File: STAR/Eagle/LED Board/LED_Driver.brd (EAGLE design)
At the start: 30.5 x 6.6 mm, 8 parts

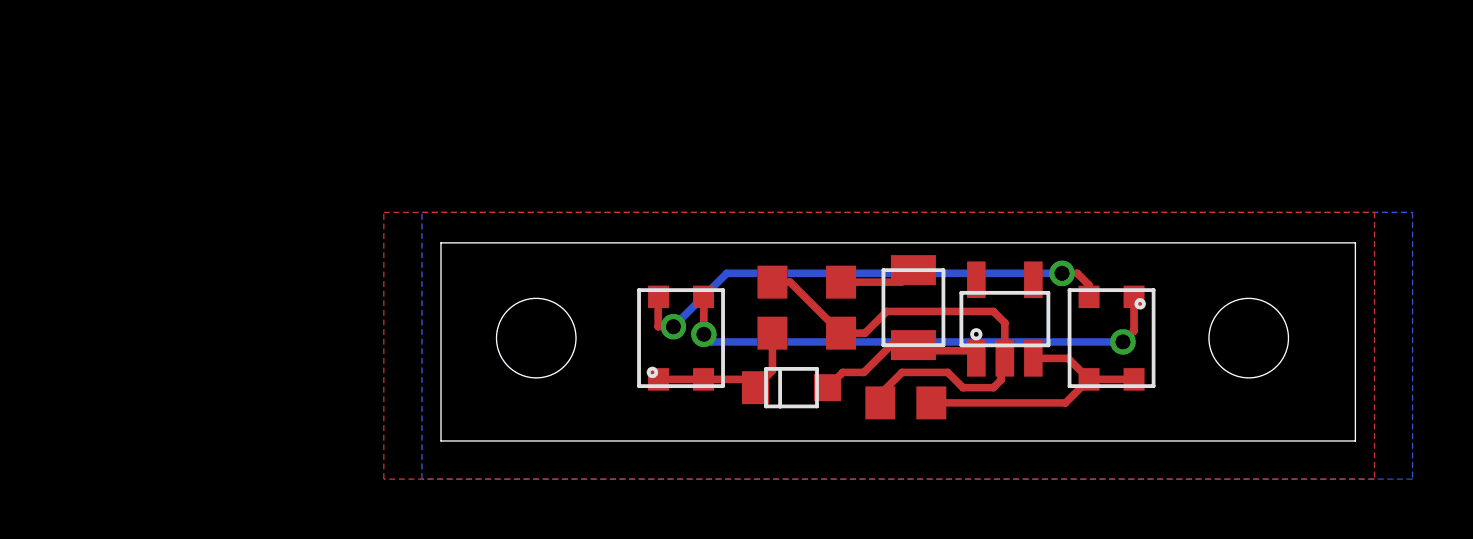
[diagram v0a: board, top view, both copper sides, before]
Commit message: LED board, added text
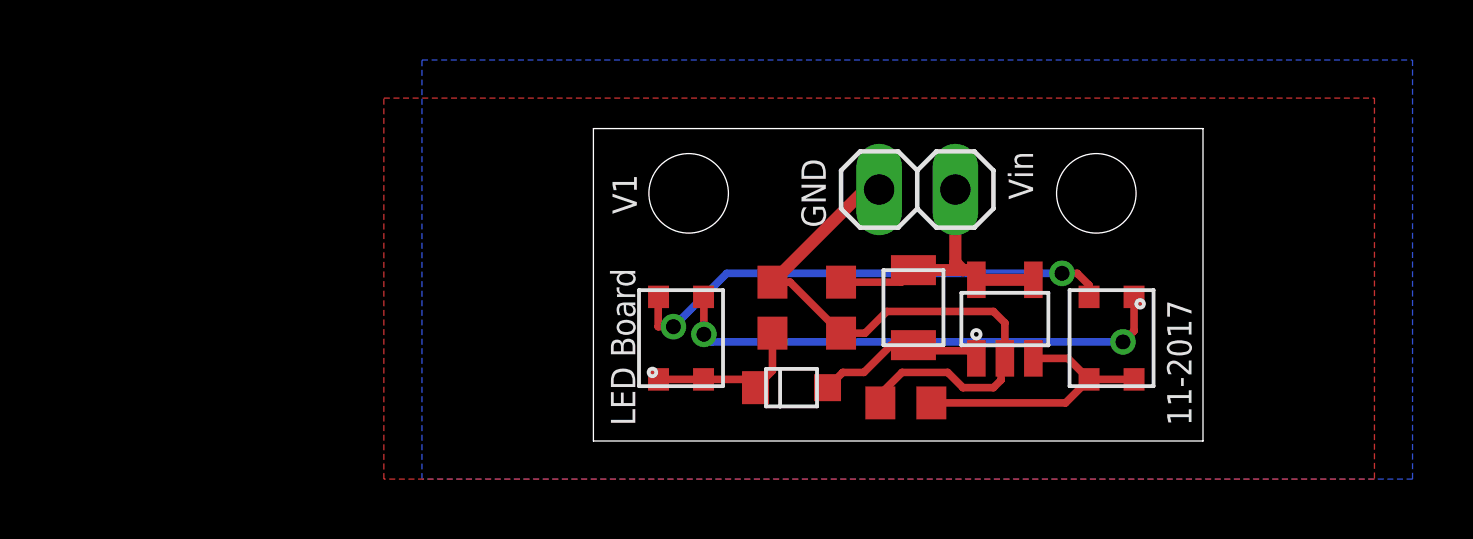
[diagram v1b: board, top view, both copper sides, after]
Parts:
- added JP1: (no value), pinhead:1X02
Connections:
- net +3V3: now also JP1.2
- net GND: now also JP1.1
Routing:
- net +3V3: track 2.91 -> 9.63 mm
- net GND: track 16.2 -> 21.0 mm
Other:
- board size 30.5 x 6.6 mm -> 20.3 x 10.4 mm
- board text added: "11-2017"
- board text added: "GND"
- board text added: "LED Board"
- board text added: "V1"
- board text added: "Vin"
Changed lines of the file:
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@@
 <layer number="98" name="Guide" color="6" fill="1" visible="no" active="no"/>
 <layer number="99" name="SpiceOrder" color="5" fill="1" visible="no" active="no"/>
+<layer number="200" name="200bmp" color="1" fill="10" visible="yes" active="yes"/>
 </layers>
 <board>
 <plain>
-<wire x1="5.715" y1="0" x2="36.195" y2="0" width="0" layer="20"/>
-<wire x1="36.195" y1="0" x2="36.195" y2="6.604" width="0" layer="20"/>
-<wire x1="36.195" y1="6.604" x2="5.715" y2="6.604" width="0" layer="20"/>
-<wire x1="5.715" y1="6.604" x2="5.715" y2="0" width="0" layer="20"/>
-<hole x="8.89" y="3.429" drill="2.65"/>
-<hole x="32.639" y="3.429" drill="2.65"/>
+<wire x1="10.795" y1="0" x2="31.115" y2="0" width="0" layer="20"/>
+<wire x1="31.115" y1="0" x2="31.115" y2="10.414" width="0" layer="20"/>
+<wire x1="31.115" y1="10.414" x2="10.795" y2="10.414" width="0" layer="20"/>
+<wire x1="10.795" y1="10.414" x2="10.795" y2="0" width="0" layer="20"/>
+<hole x="13.97" y="8.255" drill="2.65"/>
+<hole x="27.559" y="8.255" drill="2.65"/>
+<text x="24.638" y="9.652" size="0.8128" layer="21" font="vector" rot="R270">Vin</text>
+<text x="18.542" y="7.112" size="0.8128" layer="21" font="vector" rot="R90">GND</text>
+<text x="12.192" y="0.508" size="0.8128" layer="21" font="vector" rot="R90">LED Board</text>
+<text x="11.43" y="8.89" size="0.8128" layer="21" font="vector" rot="R270">V1</text>
+<text x="30.734" y="0.508" size="0.8128" layer="21" font="vector" rot="R90">11-2017</text>
 </plain>
 <attributes>
@@
 <element name="U$4" library="LED" package="CLA2A-WKW-CYBZ0343CT" value="CLA2A-WKW-CYBZ0343CT" x="13.716" y="3.429" smashed="yes" rot="R90"/>
 <element name="U$5" library="LED" package="CLA2A-WKW-CYBZ0343CT" value="CLA2A-WKW-CYBZ0343CT" x="28.067" y="3.429" smashed="yes" rot="R270"/>
+<element name="JP1" library="pinhead" package="1X02" value="" x="21.59" y="8.382" smashed="yes">
+<attribute name="VALUE" x="19.05" y="5.207" size="1.27" layer="27"/>
+</element>
 </elements>
 <signals>
@@
 <wire x1="21.063" y1="5.295" x2="21.463" y2="5.695" width="0.254" layer="1"/>
 <wire x1="23.494" y1="5.695" x2="23.561" y2="5.374" width="0.254" layer="1"/>
-<wire x1="23.561" y1="5.374" x2="25.461" y2="5.374" width="0" layer="19" extent="1-1"/>
-<wire x1="21.463" y1="5.695" x2="23.494" y2="5.695" width="0" layer="19" extent="1-1"/>
+<wire x1="23.494" y1="5.695" x2="23.114" y2="5.695" width="0.4064" layer="1"/>
+<wire x1="23.114" y1="5.695" x2="21.463" y2="5.695" width="0.4064" layer="1"/>
+<wire x1="23.561" y1="5.374" x2="25.461" y2="5.374" width="0.4064" layer="1"/>
+<contactref element="JP1" pad="2"/>
+<wire x1="22.86" y1="8.382" x2="22.86" y2="5.949" width="0.4064" layer="1"/>
+<wire x1="22.86" y1="5.949" x2="23.114" y2="5.695" width="0.4064" layer="1"/>
 </signal>
 <signal name="GND">
@@
 <wire x1="24.384" y1="2.627" x2="24.511" y2="2.754" width="0.254" layer="1"/>
 <polygon width="0.254" layer="16">
-<vertex x="5.08" y="7.62"/>
-<vertex x="38.1" y="7.62"/>
+<vertex x="5.08" y="12.7"/>
+<vertex x="38.1" y="12.7"/>
 <vertex x="38.1" y="-1.27"/>
 <vertex x="5.08" y="-1.27"/>
 </polygon>
 <polygon width="0.254" layer="1">
-<vertex x="3.81" y="7.62"/>
-<vertex x="36.83" y="7.62"/>
+<vertex x="3.81" y="11.43"/>
+<vertex x="36.83" y="11.43"/>
 <vertex x="36.83" y="-1.27"/>
 <vertex x="3.81" y="-1.27"/>
 </polygon>
+<contactref element="JP1" pad="1"/>
+<wire x1="20.32" y1="8.382" x2="19.851" y2="8.382" width="0.4064" layer="1"/>
+<wire x1="19.851" y1="8.382" x2="16.764" y2="5.295" width="0.4064" layer="1"/>
 </signal>
 <signal name="N$1">

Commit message: screws
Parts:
- C1: value (none) -> .1uF
- C2: value (none) -> 22uF
- R1: value (none) -> 4.75
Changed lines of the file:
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@@
 <wire x1="31.115" y1="10.414" x2="10.795" y2="10.414" width="0" layer="20"/>
 <wire x1="10.795" y1="10.414" x2="10.795" y2="0" width="0" layer="20"/>
-<hole x="13.97" y="8.255" drill="2.65"/>
-<hole x="27.559" y="8.255" drill="2.65"/>
+<hole x="13.97" y="8.255" drill="2.1"/>
+<hole x="27.559" y="8.255" drill="2.1"/>
 <text x="24.638" y="9.652" size="0.8128" layer="21" font="vector" rot="R270">Vin</text>
 <text x="18.542" y="7.112" size="0.8128" layer="21" font="vector" rot="R90">GND</text>
@@
 <text x="11.43" y="8.89" size="0.8128" layer="21" font="vector" rot="R270">V1</text>
 <text x="30.734" y="0.508" size="0.8128" layer="21" font="vector" rot="R90">11-2017</text>
+<circle x="13.97" y="8.255" radius="1.9" width="0.4064" layer="51"/>
+<circle x="27.559" y="8.255" radius="1.9" width="0.4064" layer="51"/>
 </plain>
 <attributes>
@@
 </autorouter>
 <elements>
-<element name="C1" library="resistor" package="C0603" value="" x="16.764" y="4.445" smashed="yes" rot="R90">
+<element name="C1" library="resistor" package="C0603" value=".1uF" x="16.764" y="4.445" smashed="yes" rot="R90">
 <attribute name="VALUE" x="18.669" y="3.81" size="1.27" layer="27" rot="R90"/>
 </element>
-<element name="C2" library="resistor" package="C0603" value="" x="19.05" y="4.445" smashed="yes" rot="R270">
+<element name="C2" library="resistor" package="C0603" value="22uF" x="19.05" y="4.445" smashed="yes" rot="R270">
 <attribute name="VALUE" x="17.145" y="5.08" size="1.27" layer="27" rot="R270"/>
 </element>
-<element name="R1" library="resistor" package="R0603" value="" x="21.209" y="1.27" smashed="yes">
+<element name="R1" library="resistor" package="R0603" value="4.75" x="21.209" y="1.27" smashed="yes">
 <attribute name="VALUE" x="20.574" y="-0.635" size="1.27" layer="27"/>
 </element>

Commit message: misc board stuff
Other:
- board text added: "1-2018"
- board text added: "V1.1"
- board text removed: "11-2017"
- board text removed: "V1"
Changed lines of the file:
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@@
 <text x="18.542" y="7.112" size="0.8128" layer="21" font="vector" rot="R90">GND</text>
 <text x="12.192" y="0.508" size="0.8128" layer="21" font="vector" rot="R90">LED Board</text>
-<text x="11.43" y="8.89" size="0.8128" layer="21" font="vector" rot="R270">V1</text>
-<text x="30.734" y="0.508" size="0.8128" layer="21" font="vector" rot="R90">11-2017</text>
+<text x="11.43" y="10.16" size="0.8128" layer="21" font="vector" rot="R270">V1.1</text>
+<text x="30.734" y="0.508" size="0.8128" layer="21" font="vector" rot="R90">1-2018</text>
 <circle x="13.97" y="8.255" radius="1.9" width="0.4064" layer="51"/>
 <circle x="27.559" y="8.255" radius="1.9" width="0.4064" layer="51"/>

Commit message: CAD for STARduino, datalogger
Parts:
- moved U$2 10.8 mm to (10.7, 4.45)
- moved U$3 10.8 mm to (6.60, 1.78)
- moved U$5 10.8 mm to (17.3, 3.43)
- moved C2 10.8 mm to (8.26, 4.45)
- moved JP1 10.8 mm to (10.8, 8.38)
- moved R1 10.8 mm to (10.4, 1.27)
- moved U$1 10.8 mm to (13.7, 4.06)
- moved U$4 10.8 mm to (2.92, 3.43)
- moved C1 10.8 mm to (5.97, 4.45)
